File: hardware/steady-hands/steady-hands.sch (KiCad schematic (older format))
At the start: 1 part

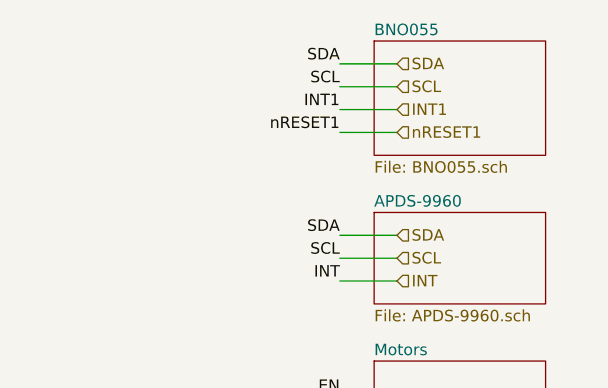
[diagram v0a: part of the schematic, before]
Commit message: Feature/bsp structure (#6)
* Adds new BSP src files for new structure since some bsp modules are used multiple times in the drivers

* Adds new BSP src files for new structure since some bsp modules are used multiple times in the drivers

* Adds new BSP src files for new structure since some bsp modules are used multiple times in the drivers

* Adds documentation to bsp src files

* Adds missing bracket
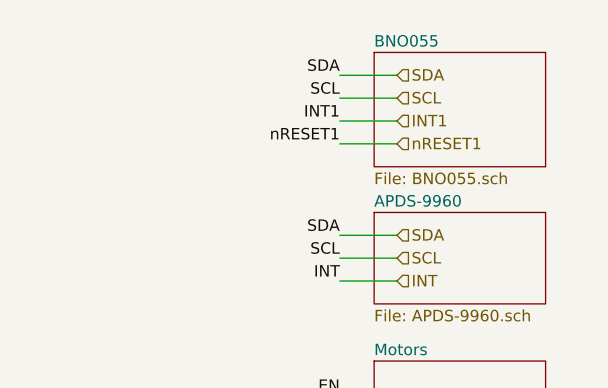
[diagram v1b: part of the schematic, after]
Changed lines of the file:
@@
 Wire Wire Line
 	6400 4050 6550 4050
-Text HLabel 9100 1550 2    50   Input ~ 0
+Text HLabel 9100 1600 2    50   Input ~ 0
 SDA
-Text HLabel 9100 1650 2    50   Input ~ 0
+Text HLabel 9100 1700 2    50   Input ~ 0
 SCL
-Text HLabel 9100 1750 2    50   Input ~ 0
+Text HLabel 9100 1800 2    50   Input ~ 0
 INT1
 $Sheet
-S 9000 1450 750  500
+S 9000 1500 750  500
 U 5EF43BAC
 F0 "BNO055" 50
@@
 $EndSheet
 Wire Wire Line
-	9100 1550 8850 1550
+	9100 1600 8850 1600
 Wire Wire Line
-	9100 1650 8850 1650
+	9100 1700 8850 1700
 Wire Wire Line
-	9100 1750 8850 1750
-Text Label 8850 1550 2    50   ~ 0
+	9100 1800 8850 1800
+Text Label 8850 1600 2    50   ~ 0
 SDA
-Text Label 8850 1650 2    50   ~ 0
+Text Label 8850 1700 2    50   ~ 0
 SCL
-Text Label 8850 1750 2    50   ~ 0
+Text Label 8850 1800 2    50   ~ 0
 INT1
 $Sheet
@@
 Text Label 8850 3800 2    50   ~ 0
 INT2
-Text HLabel 9100 1850 2    50   Input ~ 0
+Text HLabel 9100 1900 2    50   Input ~ 0
 nRESET1
 Wire Wire Line
-	9100 1850 8850 1850
-Text Label 8850 1850 2    50   ~ 0
+	9100 1900 8850 1900
+Text Label 8850 1900 2    50   ~ 0
 nRESET1
 Text Label 8850 4350 2    50   ~ 0
